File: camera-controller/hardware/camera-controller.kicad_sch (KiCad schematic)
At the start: 55 parts, among them J1 USB_C_Receptacle_USB2.0_14P, J2 Conn_Coaxial, J3 Conn_01x04, J4 Conn_01x08, U1 STM32H523RCTx, U2 LR2021, U3 MIC5504-3.3YM5, Y1 32.768MHz, Y2 24MHz, Y3 32MHz 10pF

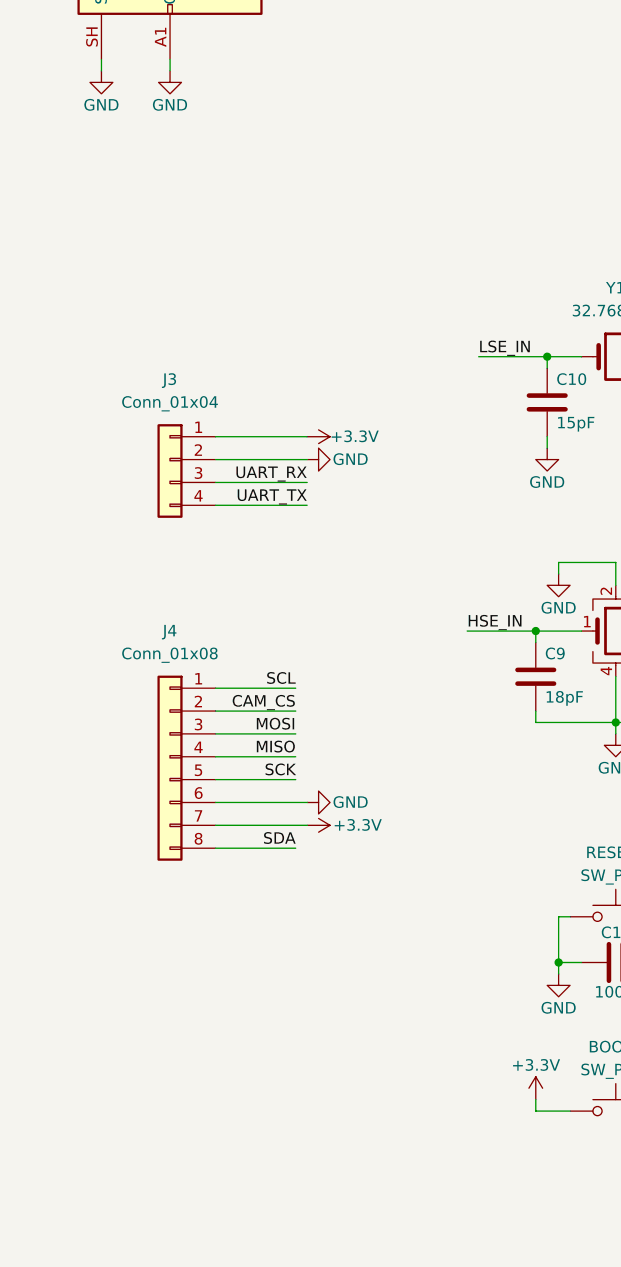
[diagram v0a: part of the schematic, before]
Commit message: added micro sd card holder
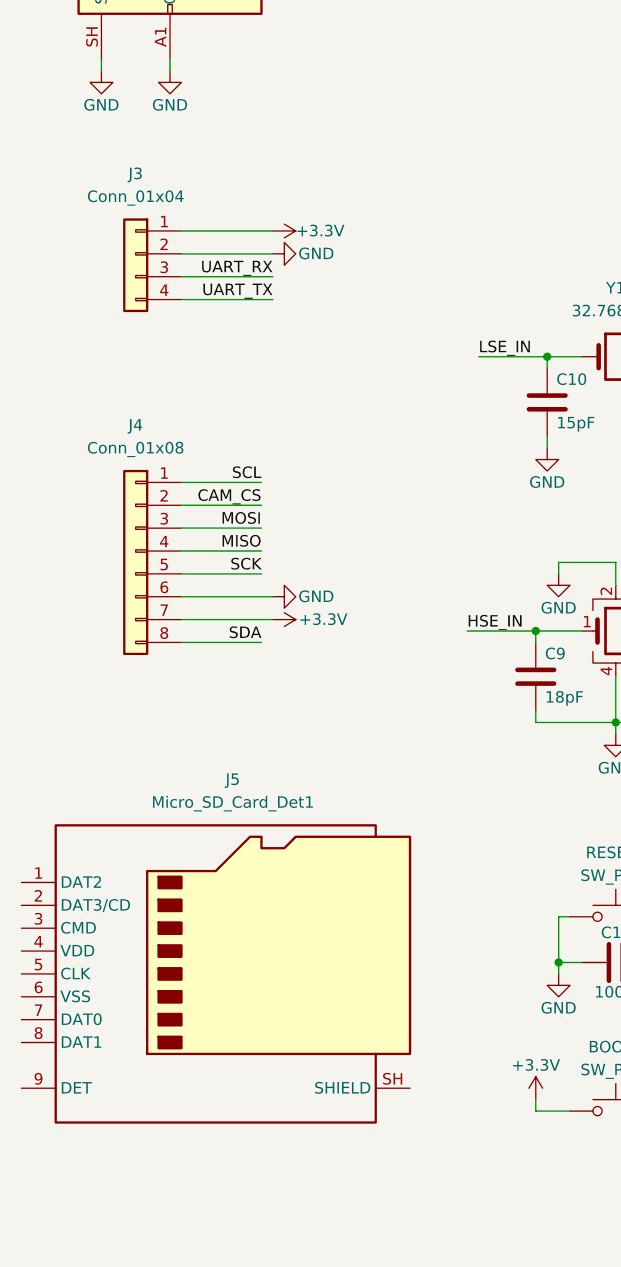
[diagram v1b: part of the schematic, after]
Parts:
- added J5: Micro_SD_Card_Det1, Connector_Card:microSD_HC_Molex_104031-0811, symbol Connector:Micro_SD_Card_Det1
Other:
- moved on the sheet: J3, J4

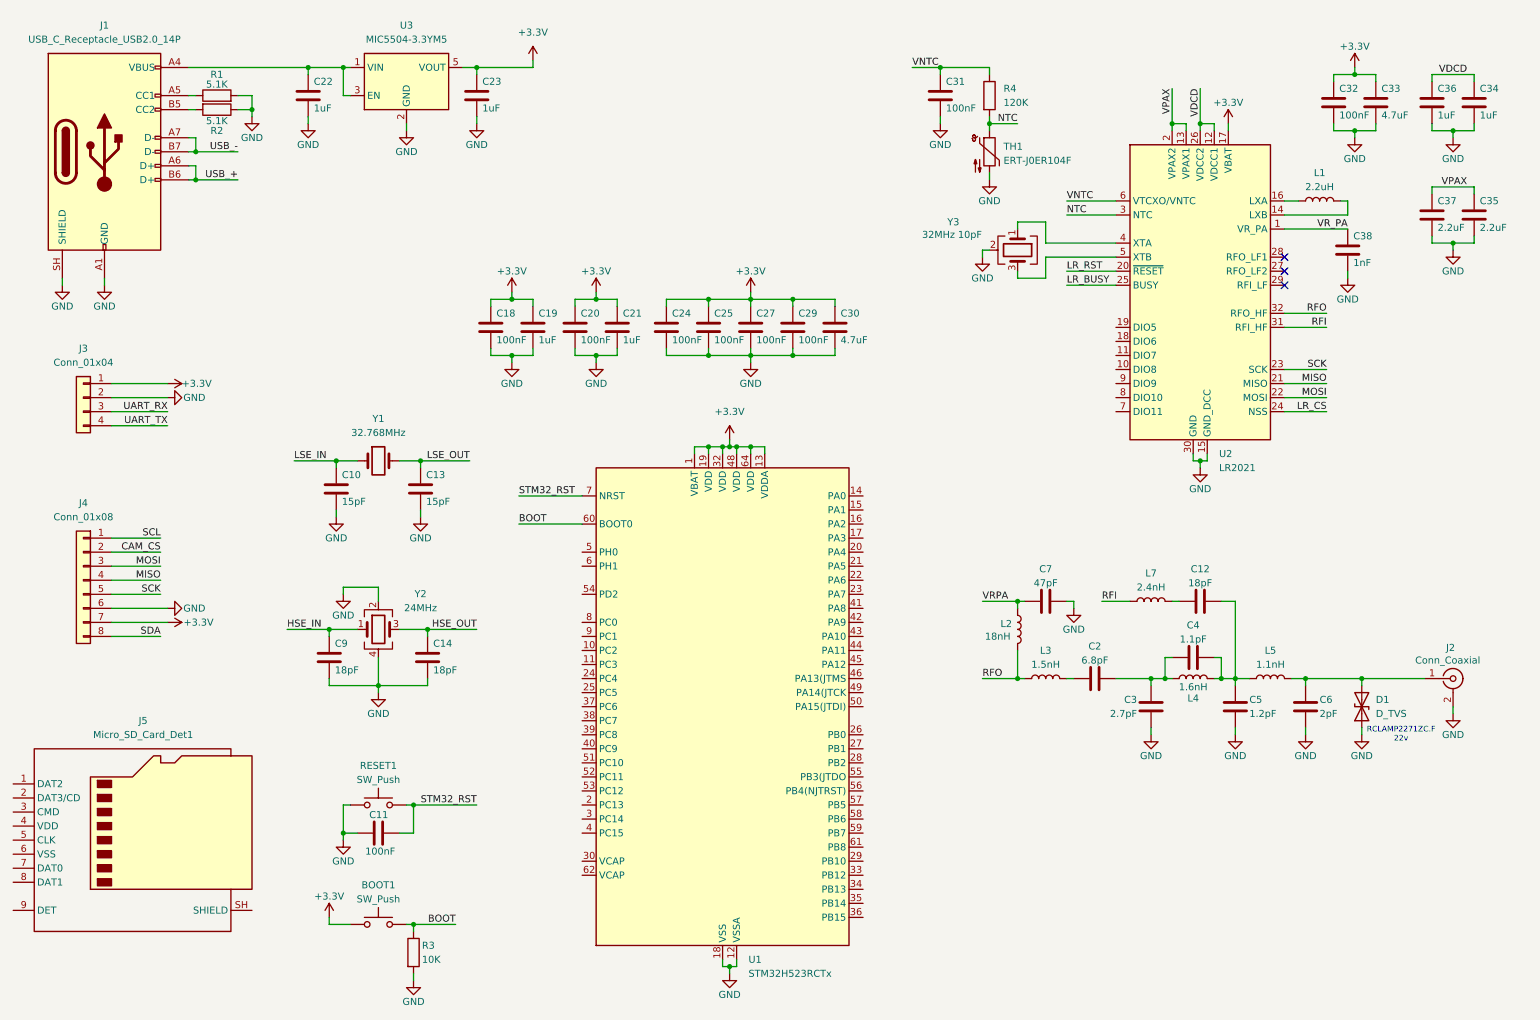
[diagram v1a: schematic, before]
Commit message: made camera controller schematic
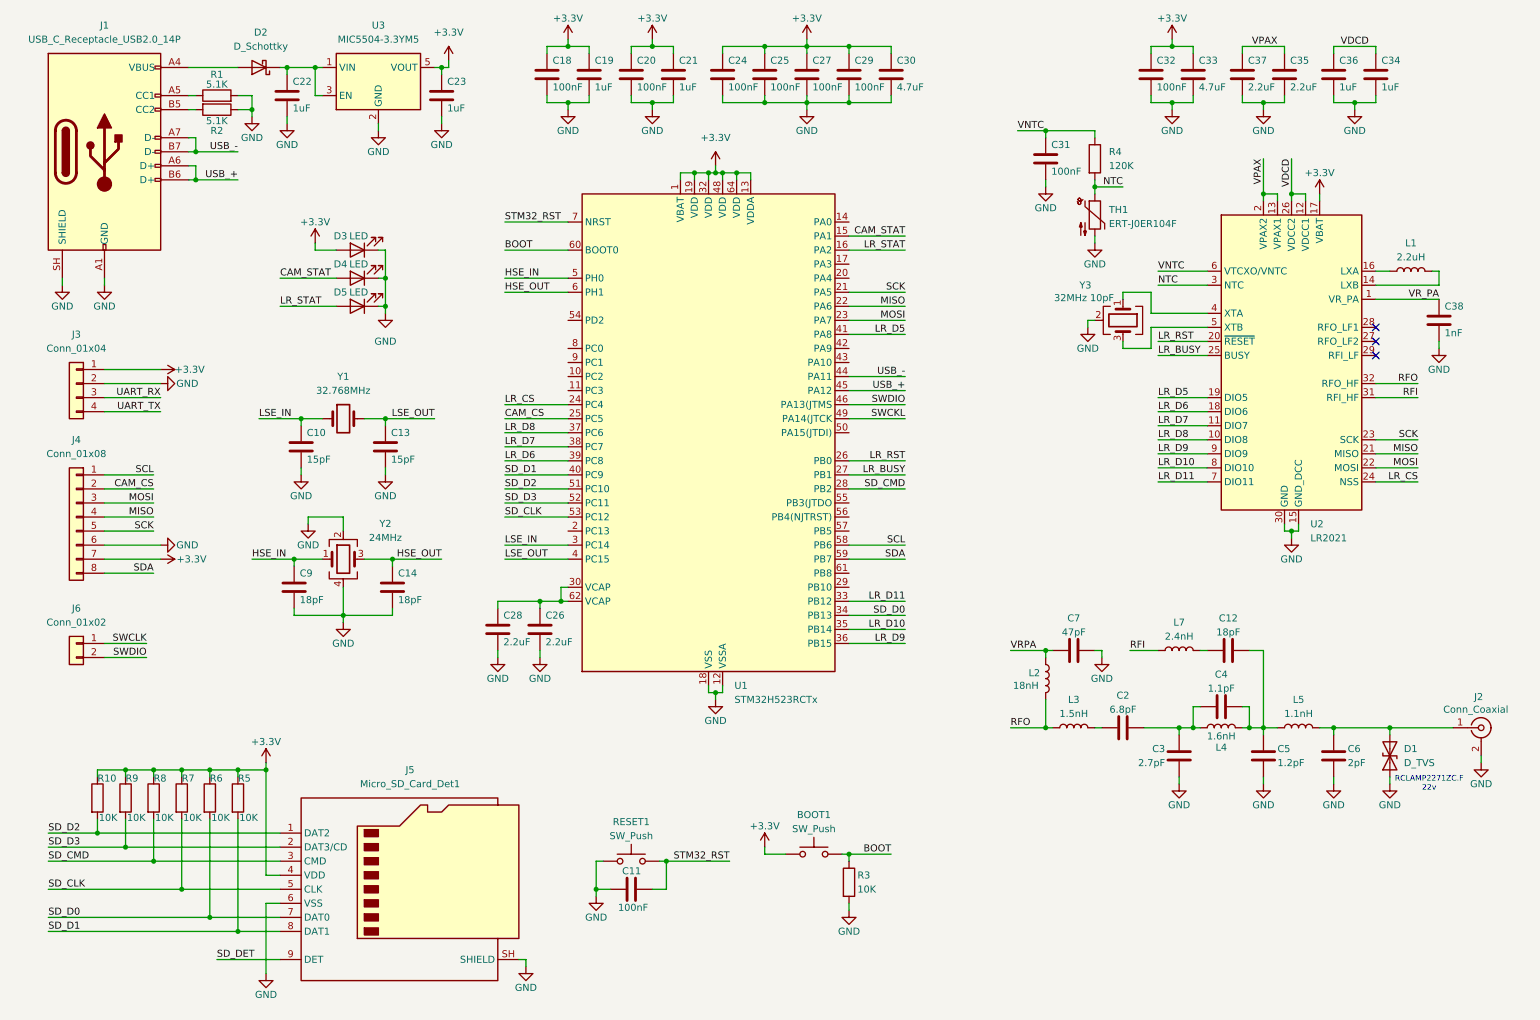
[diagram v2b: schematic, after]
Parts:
- added C26, C28: 2.2uF, Capacitor_SMD:C_0603_1608Metric, symbol Device:C
- added D2: D_Schottky, symbol Device:D_Schottky
- added D3, D4, D5: LED, symbol Device:LED
- added J6: Conn_01x02, Connector_PinHeader_2.54mm:PinHeader_1x02_P2.54mm_Vertical, symbol Connector_Generic:Conn_01x02
- added R10, R5, R6, R7, R8, R9: 10K, symbol Device:R
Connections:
- net +3.3V: now also J5.4 (VDD), D3.2 (A), R10.1, R5.1, R6.1, R7.1, R8.1, R9.1
- net CAM_CS: now also U1.25 (PC5)
- net GND: now also J5.6 (VSS), J5.SH (SHIELD), C26.2, C28.2, D3.1 (K), D4.1 (K), D5.1 (K)
- net HSE_IN: now also U1.5 (PH0)
- net HSE_OUT: now also U1.6 (PH1)
- net LR_BUSY: now also U1.27 (PB1)
- net LR_CS: now also U1.24 (PC4)
- net LR_RST: now also U1.26 (PB0)
- net LSE_IN: now also U1.3 (PC14)
- net LSE_OUT: now also U1.4 (PC15)
- net MISO: now also U1.22 (PA6)
- net MOSI: now also U1.23 (PA7)
- net SCK: now also U1.21 (PA5)
- net SCL: now also U1.58 (PB6)
- net SDA: now also U1.59 (PB7)
- net USB_+: now also U1.45 (PA12)
- net USB_-: now also U1.44 (PA11)
- net at J1.A4 (VBUS), J1.A9 (VBUS), J1.B4 (VBUS)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: now also D2.2 (A); no longer C22.1, U3.1 (VIN), U3.3 (EN)
- net CAM_STAT: now reaches U1.15 (PA1)
- net CAM_STAT: now also D4.2 (A)
- net LR_STAT: now reaches U1.16 (PA2)
- net LR_STAT: now also D5.2 (A)
- net SD_CMD: now reaches U1.28 (PB2)
- net SD_CMD: now also J5.3 (CMD), R8.2
- net at U1.30 (VCAP): now also U1.62 (VCAP), C26.1, C28.1
- net LR_D11: now reaches U1.33 (PB12)
- net LR_D11: now also U2.7 (DIO11)
- net SD_D0: now reaches U1.34 (PB13)
- net SD_D0: now also J5.7 (DAT0), R6.2
- net LR_D10: now reaches U1.35 (PB14)
- net LR_D10: now also U2.8 (DIO10)
- net LR_D9: now reaches U1.36 (PB15)
- net LR_D9: now also U2.9 (DIO9)
- net LR_D8: now reaches U1.37 (PC6)
- net LR_D8: now also U2.10 (DIO8)
- net LR_D7: now reaches U1.38 (PC7)
- net LR_D7: now also U2.11 (DIO7)
- net LR_D6: now reaches U1.39 (PC8)
- net LR_D6: now also U2.18 (DIO6)
- net SD_D1: now reaches U1.40 (PC9)
- net SD_D1: now also J5.8 (DAT1), R5.2
- net LR_D5: now reaches U1.41 (PA8)
- net LR_D5: now also U2.19 (DIO5)
- net SWDIO: now reaches U1.46 (PA13(JTMS)
- net SWDIO: now also J6.2 (Pin_2)
- net SWCKL: now reaches U1.49 (PA14(JTCK)
- net SD_D2: now reaches U1.51 (PC10)
- net SD_D2: now also J5.1 (DAT2), R10.2
- net SD_D3: now reaches U1.52 (PC11)
- net SD_D3: now also J5.2 (DAT3/CD), R9.2
- net SD_CLK: now reaches U1.53 (PC12)
- net SD_CLK: now also J5.5 (CLK), R7.2
- net SD_DET: now reaches J5.9 (DET)
- new net: C22.1, D2.1 (K), U3.1 (VIN), U3.3 (EN)
- new net SWCLK: J6.1 (Pin_1)
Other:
- moved on the sheet: BOOT1, C10, C11, C12, C13, C14, C18, C19, C2, C20, C21, C22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

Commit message: started pcb
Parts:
- added R11, R12, R13: 1.2K, Resistor_SMD:R_0402_1005Metric, symbol Device:R
- C12, C2, C3, C4, C5, C6, C7: footprint (none) -> Capacitor_SMD:C_0402_1005Metric
- C19, C21, C26, C28: footprint Capacitor_SMD:C_0603_1608Metric -> Capacitor_SMD:C_0402_1005Metric
- D1: footprint (none) -> Diode_SMD:D_0402_1005Metric
- D2: footprint (none) -> Diode_SMD:D_SOD-123
- D3, D4, D5: footprint (none) -> LED_SMD:LED_0603_1608Metric
- J1: footprint (none) -> Connector_USB:USB_C_Receptacle_HRO_TYPE-C-31-M-12
- J2: footprint (none) -> Connector_Coaxial:U.FL_Molex_MCRF_73412-0110_Vertical
- J5: footprint Connector_Card:microSD_HC_Molex_104031-0811 -> camera-controller:CUI_MSD-4-A
- L1: footprint (none) -> Inductor_SMD:L_0603_1608Metric
- L2, L3, L4, L5, L7: footprint (none) -> Inductor_SMD:L_0402_1005Metric
- R1, R10, R2, R4, R5, R6, R7, R8, R9: footprint (none) -> Resistor_SMD:R_0402_1005Metric
- Y3: footprint (none) -> Crystal:Crystal_SMD_2016-4Pin_2.0x1.6mm
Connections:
- net +3.3V: now also R11.1; no longer D3.2 (A)
- net CAM_STAT: now also R12.1; no longer D4.2 (A)
- net LR_STAT: now also R13.1; no longer D5.2 (A)
- net SD_DET: now also U1.54 (PD2)
- net at C26.1, U1.62 (VCAP): no longer C28.1, U1.30 (VCAP)
- new net: D4.2 (A), R12.2
- new net: D3.2 (A), R11.2
- new net: D5.2 (A), R13.2
- new net: C28.1, U1.30 (VCAP)
- no-connect marks 3 -> 18
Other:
- note added: "RCLAMP2261PW.C 22v"
- note removed: "RCLAMP2271ZC.F 22v"
- moved on the sheet: D3, D4, D5

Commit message: made camera controller pcb layout
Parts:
- U2: footprint Package_DFN_QFN:QFN-32-1EP_4x4mm_P0.4mm_EP2.65x2.65mm -> Package_DFN_QFN:QFN-32-1EP_7x7mm_P0.65mm_EP4.65x4.65mm
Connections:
- net SWCKL is gone; now on net SWCLK: U1.49 (PA14(JTCK)
- net VRPA is gone; now on net VR_PA: C7.1, L2.1
- net CAM_STAT: now also U1.14 (PA0); no longer U1.15 (PA1)
- net LR_BUSY: now also U1.16 (PA2); no longer U1.27 (PB1)
- net LR_CS: now also U1.17 (PA3); no longer U1.24 (PC4)
- net LR_D5: now also U1.26 (PB0); no longer U1.41 (PA8)
- net LR_D6: now also U1.27 (PB1); no longer U1.39 (PC8)
- net LR_RST: now also U1.24 (PC4); no longer U1.26 (PB0)
- net LR_STAT: now also U1.15 (PA1); no longer U1.16 (PA2)
- net UART_RX: now also U1.42 (PA9)
- net UART_TX: now also U1.43 (PA10)
- no-connect marks 18 -> 17

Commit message: finished camera controller pcb
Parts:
- removed C22, C23: 1uF, Capacitor_SMD:C_0402_1005Metric, symbol Device:C
- removed D2: D_Schottky, Diode_SMD:D_SOD-123, symbol Device:D_Schottky
- removed J1: USB_C_Receptacle_USB2.0_14P, Connector_USB:USB_C_Receptacle_HRO_TYPE-C-31-M-12, symbol Connector:USB_C_Receptacle_USB2.0_14P
- removed R1, R2: 5.1K, Resistor_SMD:R_0402_1005Metric, symbol Device:R
- removed U3: MIC5504-3.3YM5, Package_TO_SOT_SMD:SOT-23-5, symbol Regulator_Linear:MIC5504-3.3YM5
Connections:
- net VDCD renamed VDCC1
- net VDCC1: no longer C36.1, U2.26 (VDCC2)
- net VPAX renamed VPAX1
- net VPAX1: no longer C37.1, U2.2 (VPAX2)
- new net VDCC2: C36.1, U2.26 (VDCC2)
- new net VPAX2: C37.1, U2.2 (VPAX2)
